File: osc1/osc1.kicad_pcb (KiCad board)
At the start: 2 copper layers, 50.8 x 131.5 mm, 58 parts, among them J1 LinFM, J10 PWMControl, J2 Hard Sync +, J3 Hard Sync -, J4 VOct, J5 Soft Sync Input, J6 Conn_02x08_Odd_Even, J7 Triangular Wave Output, J8 Square Wave Output, J9 Saw Wave Output, U1 AS3340, U2 TL072, U3 TL072

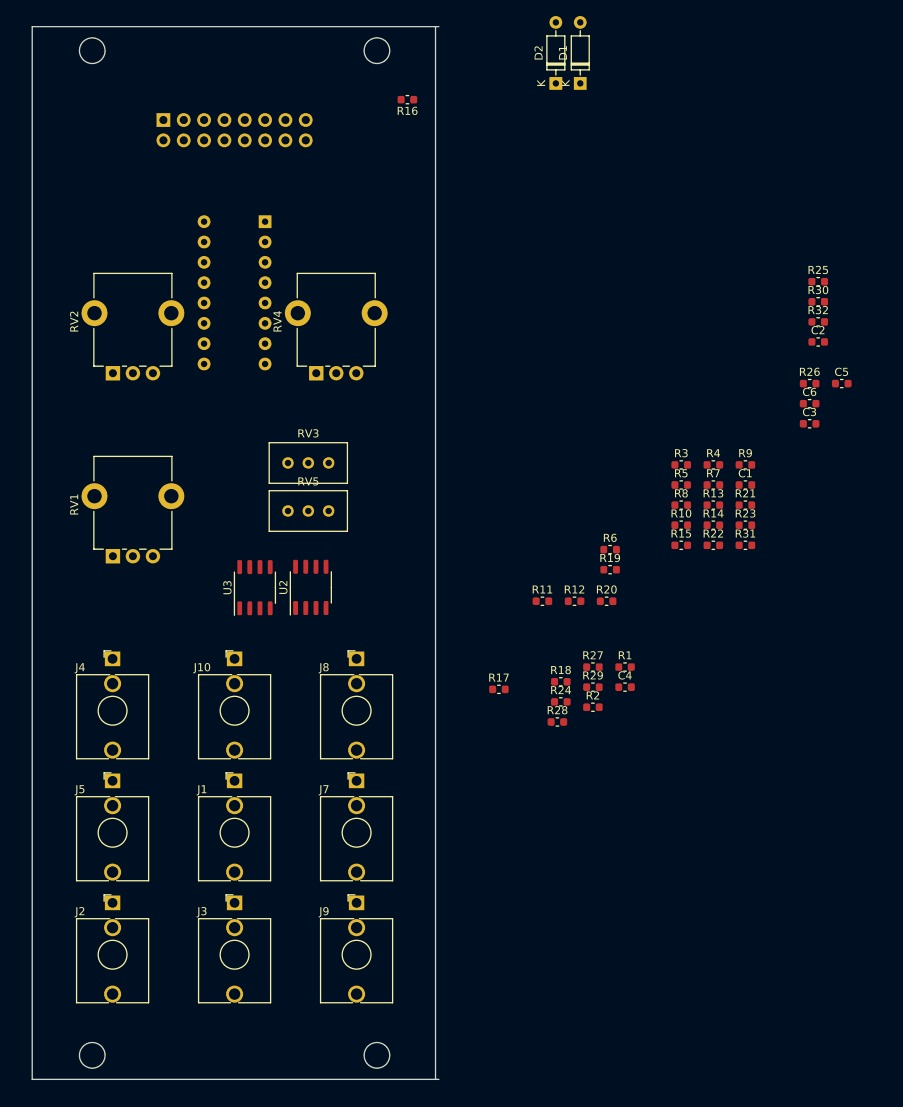
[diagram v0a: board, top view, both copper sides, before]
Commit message: osc1: plan component placement
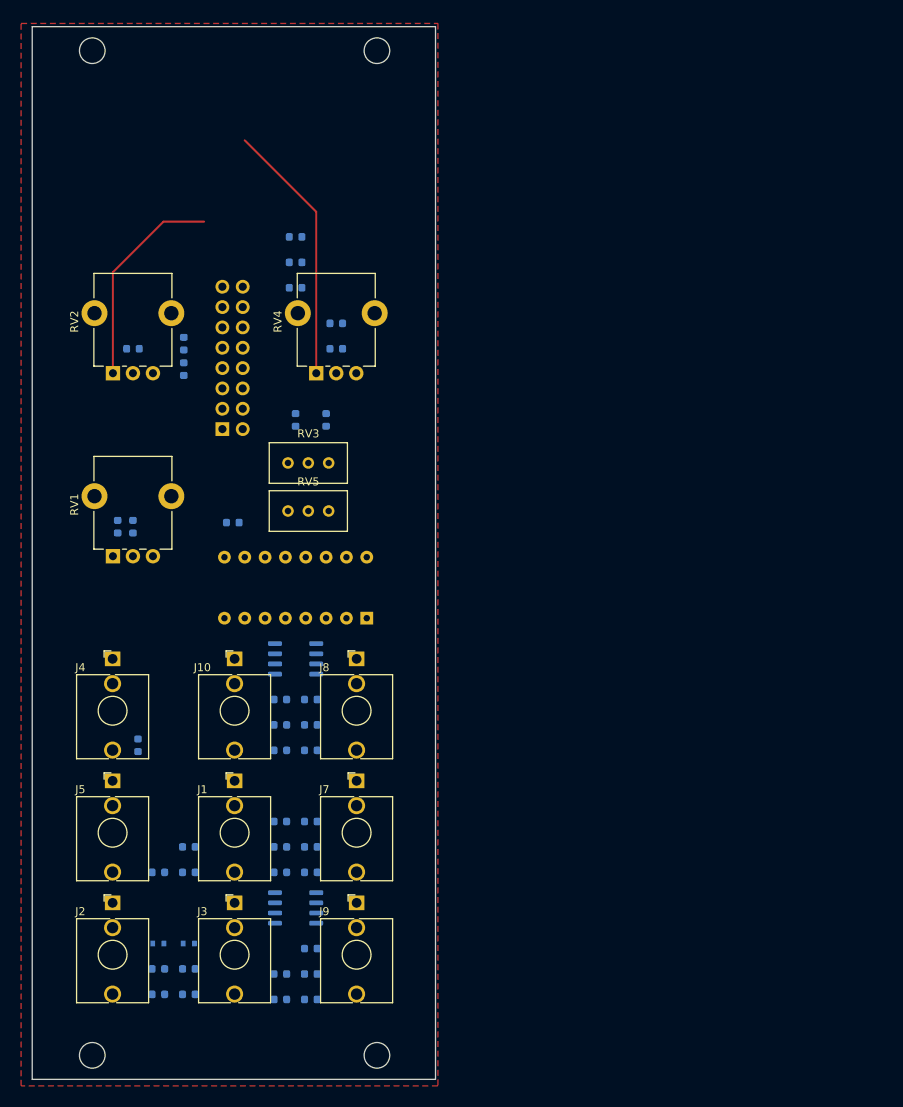
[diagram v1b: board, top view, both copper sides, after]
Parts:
- C1, C2, C3, C4, C5, C6, R1, R10, R11, R12, R13, R14, R15, R16, R17, R18, R19, R2, R20, R21, R22, R23, R24, R25, R26, R27, R28, R29, R3, R30, R31, R32, R4, R5, R6, R7, R8, R9, U2, U3: moved to B.Cu
- D1, D2: footprint Diode_THT:D_DO-35_SOD27_P7.62mm_Horizontal -> Diode_SMD:D_SOD-523; moved to B.Cu
- moved D1 119.7 mm to (84.5, 163.8), turned to 180 degrees
- moved D2 116.8 mm to (88.3, 163.8), turned to 180 degrees
- moved C2 115.9 mm to (84.5, 170.2), turned to 180 degrees
- moved R32 105.7 mm to (103.5, 170.8), turned to 180 degrees
- moved C3 105.3 mm to (88.3, 170.2), turned to 180 degrees
- moved C6 100.2 mm to (84.5, 154.9), turned to 180 degrees
- moved R26 96.6 mm to (103.5, 167.6), turned to 180 degrees
- moved R30 95.4 mm to (103.5, 154.9), turned to 180 degrees
- moved R4 93.7 mm to (84.5, 167.0), turned to 180 degrees
- moved R16 91.6 mm to (99.7, 148.6)
- moved R25 87.1 mm to (99.7, 136.5), turned to 180 degrees
- moved R5 86.2 mm to (88.3, 167.0), turned to 180 degrees
- moved C1 84.7 mm to (88.3, 154.9), turned to 180 degrees
- moved C5 82.2 mm to (87.6, 92.1), turned to 90 degrees
- moved R3 77.9 mm to (88.3, 151.8), turned to 180 degrees
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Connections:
- J10 pad S: (no net) -> GND
- J10 pad T: (no net) -> Net-(J10-PadT)
- J10 pad TN: (no net) -> +5V
- J4 pad TN: (no net) -> Net-(J4-PadTN)
- J7 pad TN: (no net) -> Net-(J7-PadTN)
- J8 pad TN: (no net) -> Net-(J8-PadTN)
- J9 pad TN: (no net) -> Net-(J9-PadTN)
- R1 pad 1: Net-(R1-Pad1) -> GND
- R1 pad 2: +12V -> PWMCTL
- R2 pad 1: Net-(R2-Pad1) -> +5V
- RV1 pad 1: Net-(R1-Pad1) -> Net-(J10-PadT)
- RV1 pad 2: Net-(R2-Pad1) -> PWMCTL
- U2 pad 4: (no net) -> Net-(U2-Pad4)
- U2 pad 8: (no net) -> Net-(U2-Pad8)
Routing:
- net +12V: track 0.08 -> 59.5 mm
- added copper zone on F.Cu, net GND
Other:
- board size 50.8 x 131.5 mm -> 50.4 x 131.5 mm

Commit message: osc1: all but 6 traces routed (crudely)
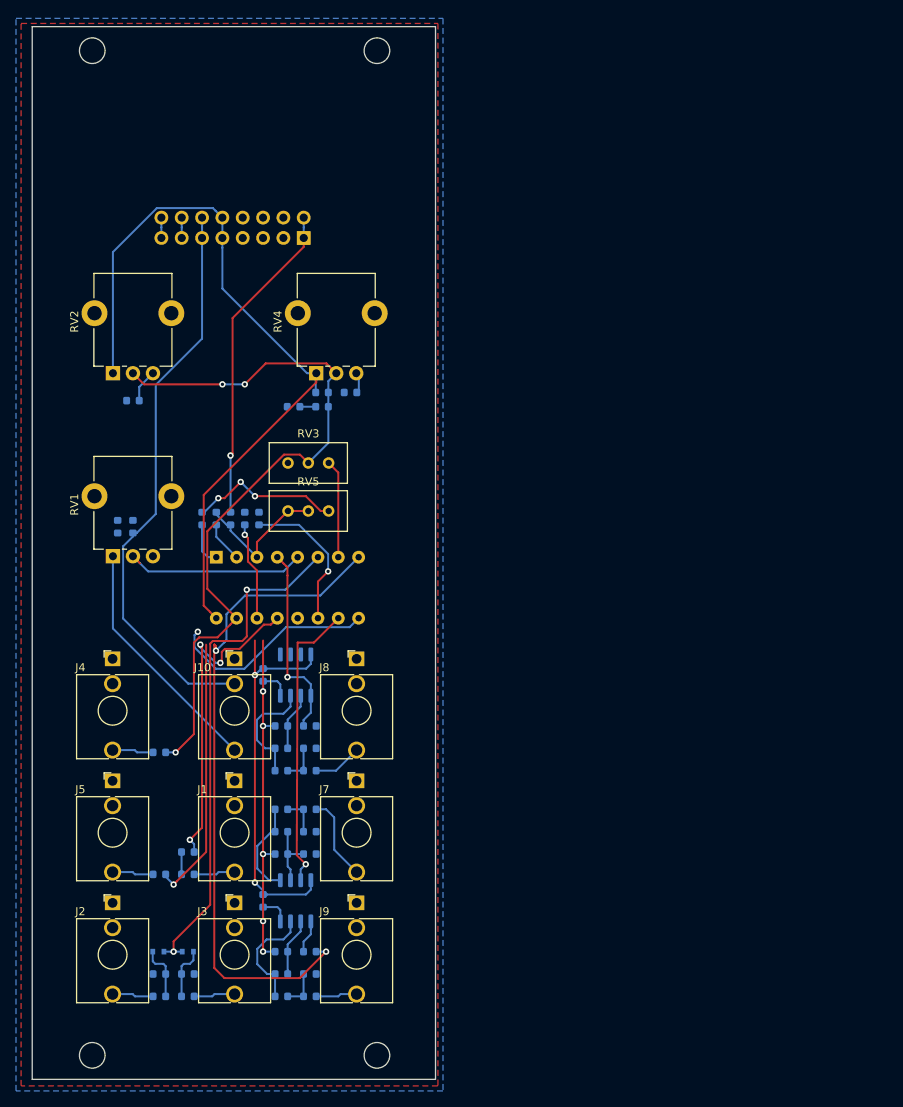
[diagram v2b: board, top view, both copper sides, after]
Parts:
- added C7: 0.1u, Capacitor_SMD:C_0603_1608Metric, B.Cu at (97.5, 130.3)
- added C8: 0.1u, Capacitor_SMD:C_0603_1608Metric, B.Cu at (97.5, 158.5)
- moved R19 53.9 mm to (99.8, 164.8)
- moved R14 36.1 mm to (93.5, 110.7), turned to 90 degrees
- moved R11 34.1 mm to (89.9, 110.7), turned to 90 degrees
- moved R12 30.5 mm to (91.7, 110.7), turned to 90 degrees
- moved J6 25.9 mm to (102.6, 75.7), turned to 90 degrees
- moved R13 23.1 mm to (95.2, 110.7), turned to 90 degrees
- moved C5 20.9 mm to (97.0, 110.7)
- moved U1 20.3 mm to (91.7, 115.6), turned to 270 degrees
- moved R9 8.82 mm to (108.5, 95.0), turned to 0 degrees
- moved R24 7.88 mm to (99.8, 147.1)
- moved R30 7.88 mm to (103.4, 147.1)
- moved R23 7.12 mm to (99.8, 139.4), turned to 0 degrees
- moved R8 6.48 mm to (81.3, 96.0), turned to 0 degrees
- moved R7 5.74 mm to (104.9, 95.0)
- moved R25 5.72 mm to (99.8, 142.2)
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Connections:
- U2 pad 4: Net-(U2-Pad4) -> -12V
- U2 pad 8: Net-(U2-Pad8) -> +12V
- U3 pad 1: Net-(R23-Pad1) -> (no net)
- U3 pad 2: Net-(R18-Pad1) -> (no net)
- U3 pad 3: PULSOUT -> (no net)
- U3 pad 4: (no net) -> -12V
- U3 pad 5: (no net) -> PULSOUT
- U3 pad 6: (no net) -> Net-(R18-Pad1)
- U3 pad 7: (no net) -> Net-(R23-Pad1)
- U3 pad 8: (no net) -> +12V
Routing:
- net Net-(R10-Pad1): track 0.00 -> 92.5 mm, vias 0 -> 3
- net +12V: track 59.5 -> 150.1 mm, vias 0 -> 5
- net -12V: track 0.00 -> 88.9 mm, vias 0 -> 3
- net SAWOUT: track 0.00 -> 82.9 mm, vias 0 -> 2
- net +5V: track 0.00 -> 71.7 mm
- net HARDSYNC: track 0.00 -> 64.0 mm, vias 0 -> 2
- net SOFTSYNC: track 0.00 -> 59.7 mm, vias 0 -> 2
- net LINFM: track 0.00 -> 40.5 mm, vias 0 -> 3
- net TRIOUT: track 0.00 -> 36.8 mm, vias 0 -> 1
- net Net-(J10-PadT): track 0.00 -> 30.5 mm
- net PULSOUT: track 0.00 -> 24.4 mm, vias 0 -> 1
- net PWMCTL: track 0.00 -> 23.4 mm
- net Net-(R11-Pad2): track 0.00 -> 18.9 mm, vias 0 -> 3
- net Net-(C5-Pad1): track 0.00 -> 18.7 mm, vias 0 -> 1
- net Net-(R12-Pad2): track 0.00 -> 17.9 mm
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- added copper zone on B.Cu, net GND

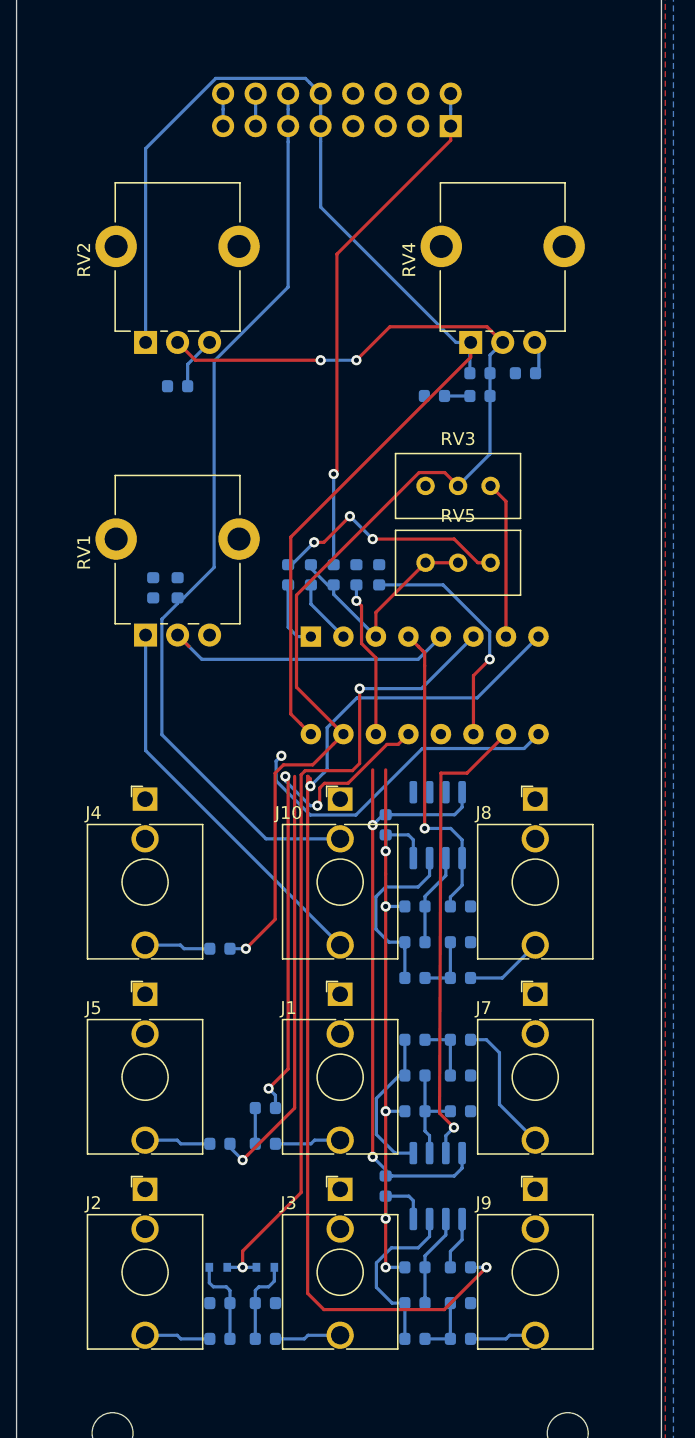
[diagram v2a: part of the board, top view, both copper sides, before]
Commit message: osc1: routed +12V, -12V and +5V
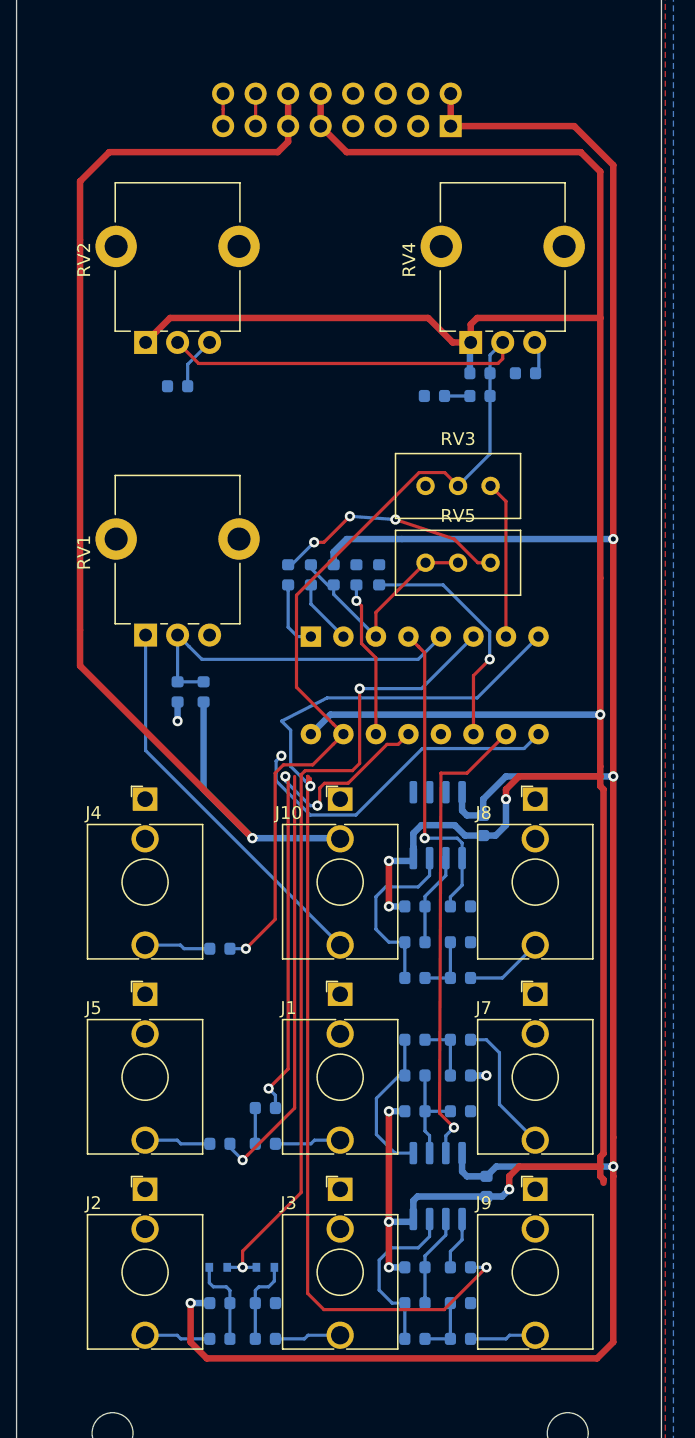
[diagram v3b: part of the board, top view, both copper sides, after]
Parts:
- moved R2 8.38 mm to (83.3, 119.9)
- moved R1 8.35 mm to (81.3, 119.9)
- moved C8 7.87 mm to (105.4, 158.5)
- moved C7 7.62 mm to (105.2, 130.3)
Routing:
- net -12V: track 88.9 -> 199.4 mm, vias 3 -> 4
- net +12V: track 150.1 -> 231.5 mm, vias 5 -> 8
- net +5V: track 71.7 -> 97.3 mm, vias 0 -> 1
- net PWMCTL: track 23.4 -> 27.8 mm
- net SAWOUT: track 82.9 -> 86.9 mm
- net GND: track 0.00 -> 2.74 mm, vias 0 -> 2
- net Net-(R10-Pad1): track 92.5 -> 92.4 mm, vias 3 -> 1
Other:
- net class Power added: clearance 0.2, trace_width 0.508, via_dia 0.8, via_drill 0.4

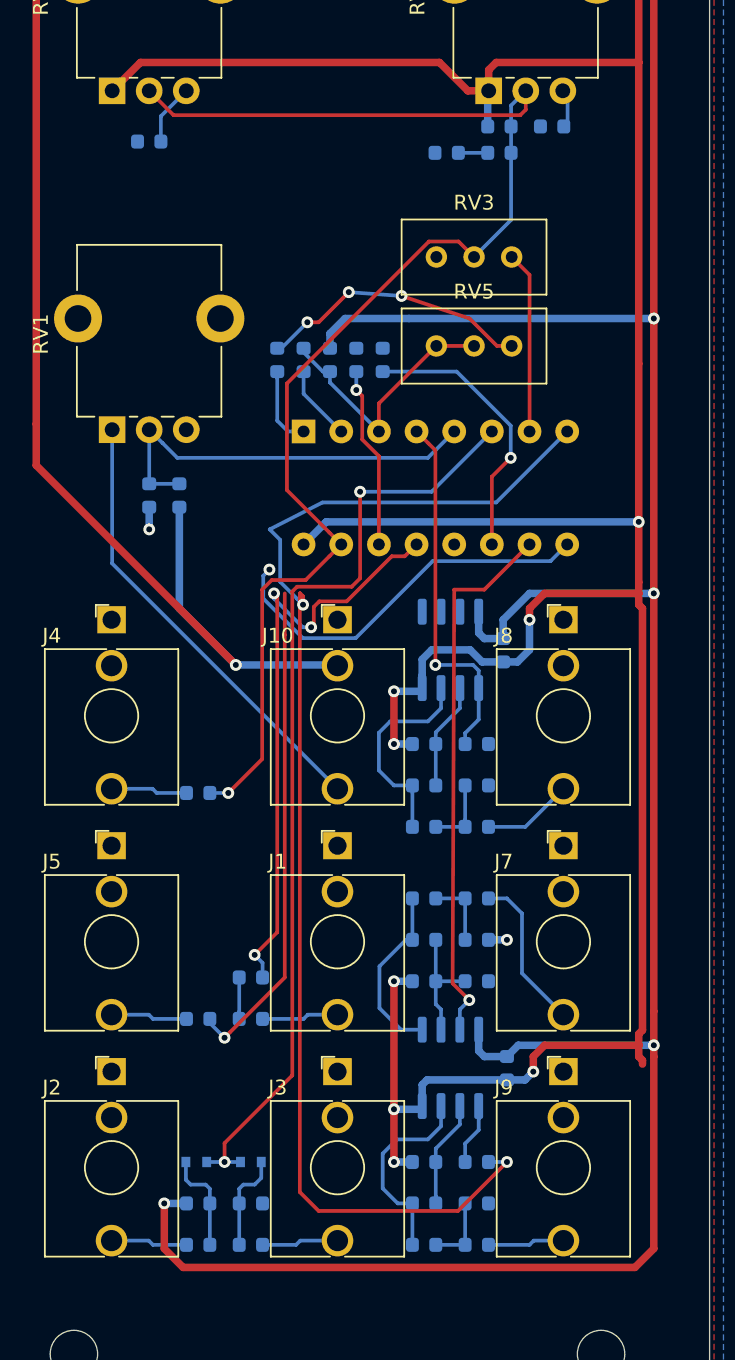
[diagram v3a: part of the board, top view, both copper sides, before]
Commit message: osc1: all nets routed, drc pass
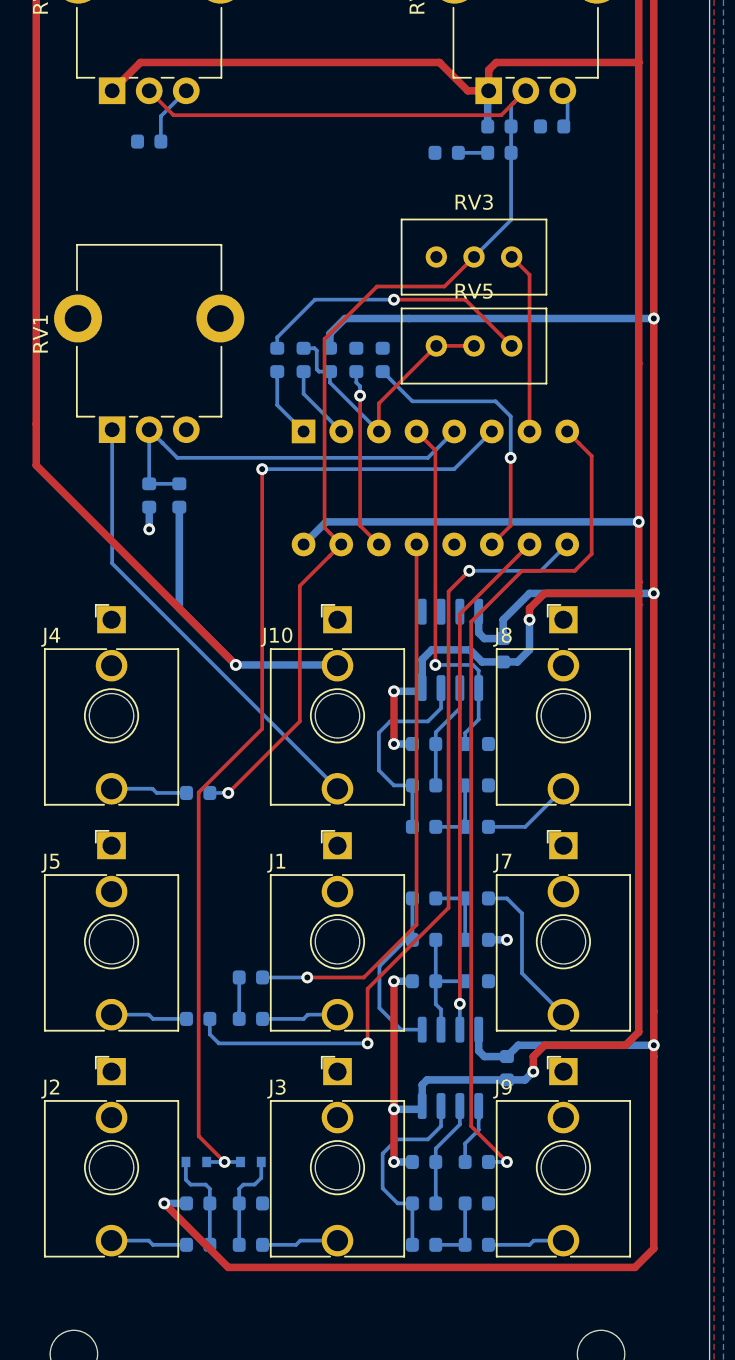
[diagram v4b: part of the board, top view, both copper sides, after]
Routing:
- net SAWOUT: track 86.9 -> 57.7 mm, vias 2 -> 1
- net SOFTSYNC: track 59.7 -> 54.0 mm
- net Net-(R10-Pad1): track 92.4 -> 87.7 mm
- net HARDSYNC: track 64.0 -> 68.1 mm
- net LINFM: track 40.5 -> 37.5 mm, vias 3 -> 1
- net +12V: track 231.5 -> 229.4 mm
- net TRIOUT: track 36.8 -> 34.7 mm
- net -12V: track 199.4 -> 197.7 mm
- net Net-(R11-Pad1): track 5.39 -> 4.77 mm
- net Net-(R12-Pad2): track 17.9 -> 18.5 mm
- net Net-(R11-Pad2): track 18.4 -> 18.9 mm, vias 3 -> 1
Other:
- outline, holes or cut-outs redrawn
